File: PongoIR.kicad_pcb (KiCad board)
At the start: 2 copper layers, 70 x 35 mm, 67 parts, among them J1 Conn_01x04, J2 Conn_01x06, Q1 BC817, Q2 2N7002, Q3 2N7002, Q4 2N7002, Q5 2N7002, SW1 Reset, SW2 Learn, SW3 Shuffle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

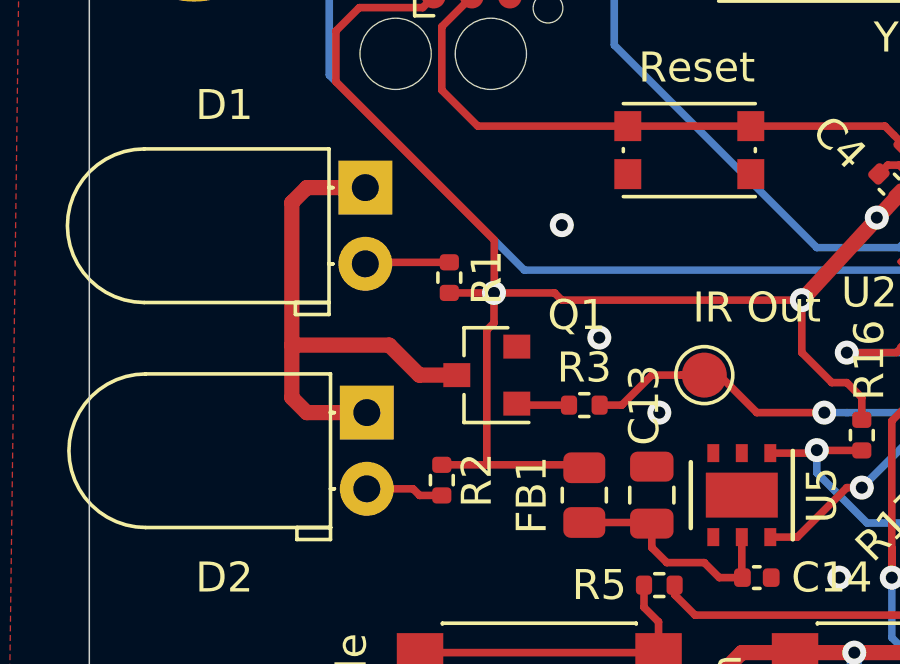
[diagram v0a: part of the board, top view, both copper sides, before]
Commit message: change IR leds to NPN transistor
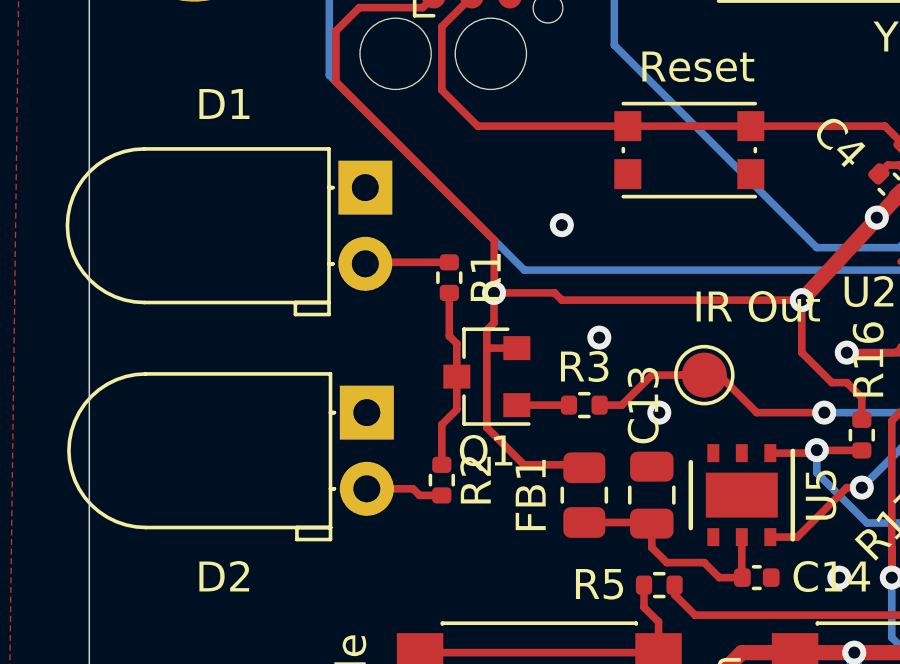
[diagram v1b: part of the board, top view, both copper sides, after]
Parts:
- Q1: value BC817 -> BC807
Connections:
- D1 pad 1: Net-(D1-Pad1) -> GND
- D2 pad 1: Net-(D1-Pad1) -> GND
- J2 pad 6: (no net) -> Net-(J2-Pad6)
- Q1 pad 2: GND -> +3V3
- Q1 pad 3: Net-(D1-Pad1) -> Net-(Q1-Pad3)
- R1 pad 1: +3V3 -> Net-(Q1-Pad3)
- R2 pad 1: +3V3 -> Net-(Q1-Pad3)
- U2 pad 10: (no net) -> Net-(U2-Pad10)
- U2 pad 14: (no net) -> Net-(U2-Pad14)
- U2 pad 15: (no net) -> Net-(U2-Pad15)
- U2 pad 17: (no net) -> Net-(U2-Pad17)
- U2 pad 18: (no net) -> Net-(U2-Pad18)
- U2 pad 19: (no net) -> Net-(U2-Pad19)
- U2 pad 2: (no net) -> Net-(U2-Pad2)
- U2 pad 20: (no net) -> Net-(U2-Pad20)
- U2 pad 25: (no net) -> Net-(U2-Pad25)
- U2 pad 26: (no net) -> Net-(U2-Pad26)
- U2 pad 27: (no net) -> Net-(U2-Pad27)
- U2 pad 28: (no net) -> Net-(U2-Pad28)
- U2 pad 3: (no net) -> Net-(U2-Pad3)
- U2 pad 35: (no net) -> Net-(U2-Pad35)
- U2 pad 38: (no net) -> Net-(U2-Pad38)
- U2 pad 39: (no net) -> Net-(U2-Pad39)
- U2 pad 4: (no net) -> Net-(U2-Pad4)
- U2 pad 40: (no net) -> Net-(U2-Pad40)
- U2 pad 41: (no net) -> Net-(U2-Pad41)
- U2 pad 42: (no net) -> Net-(U2-Pad42)
- U2 pad 43: (no net) -> Net-(U2-Pad43)
- U2 pad 45: (no net) -> Net-(U2-Pad45)
- U4 pad 1: (no net) -> Net-(U4-Pad1)
- U4 pad 2: (no net) -> Net-(U4-Pad2)
- U4 pad 3: (no net) -> Net-(U4-Pad3)
- U5 pad 3: (no net) -> Net-(U5-Pad3)
- U5 pad 4: (no net) -> Net-(U5-Pad4)
- U5 pad 7: (no net) -> Net-(U5-Pad7)
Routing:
- net Net-(D1-Pad1): track 17.8 -> 0.00 mm
- net Net-(Q1-Pad3): track 0.00 -> 6.04 mm
- net +3V3: track 253.6 -> 250.9 mm
